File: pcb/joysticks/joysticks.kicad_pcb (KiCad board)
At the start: 2 copper layers, 25 x 25 mm, 12 parts, among them J1001 Conn_01x01_Socket, J1007 Conn_01x01_Socket

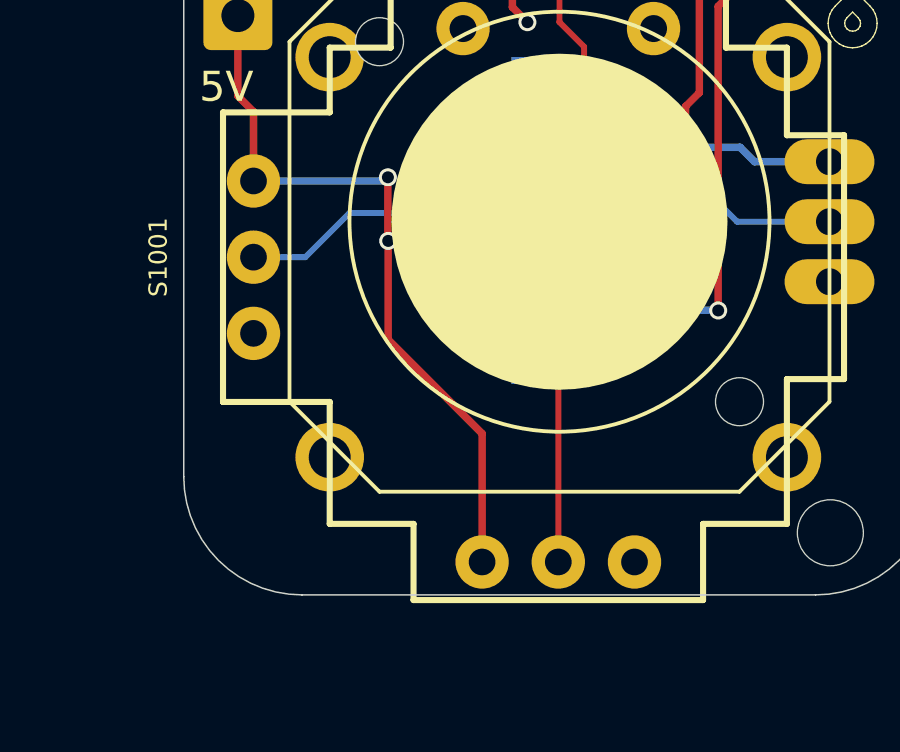
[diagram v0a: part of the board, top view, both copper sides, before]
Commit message: added joycon connector to joysticks module
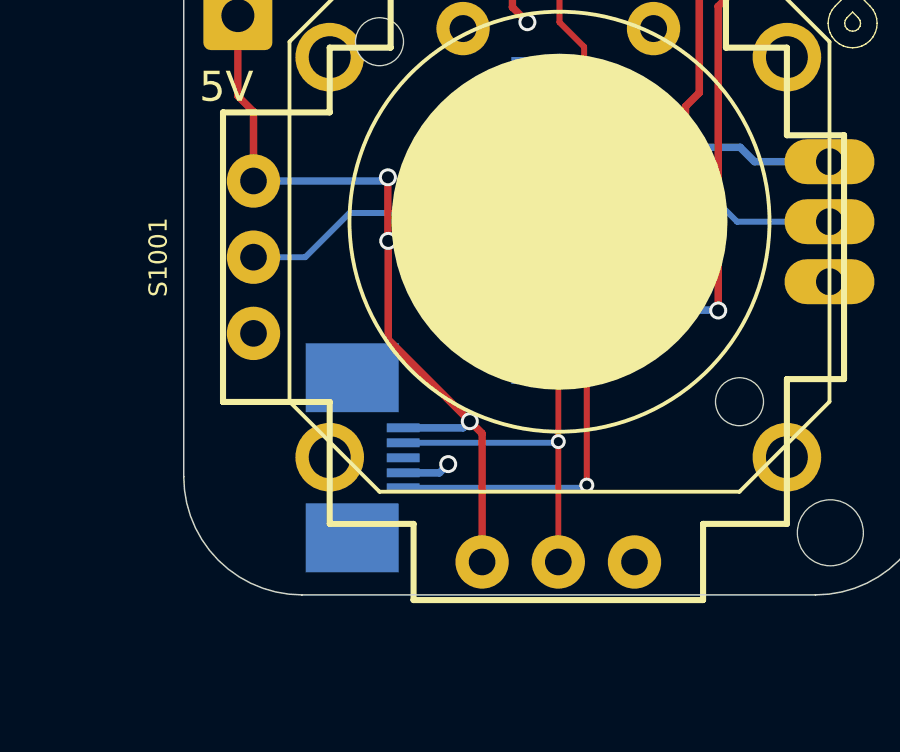
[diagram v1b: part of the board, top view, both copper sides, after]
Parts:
- added J1002: Conn_01x05_Socket, Connector_FFC-FPC:TE_0-1734839-5_1x05-1MP_P0.5mm_Horizontal, B.Cu at (75.0, 118.7)
- moved REF** 7.77 mm to (84.9, 116.5)
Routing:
- net GPIO_AD1: track 20.7 -> 35.9 mm, vias 1 -> 2
- net GPIO_AD2: track 25.5 -> 30.7 mm, vias 1 -> 2
- net VDD_5V: track 52.2 -> 54.5 mm, vias 5 -> 6
- net GND: track 8.09 -> 9.71 mm, vias 3 -> 4
